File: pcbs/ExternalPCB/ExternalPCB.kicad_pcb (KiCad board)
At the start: 2 copper layers, 58.4 x 127 mm, 31 parts, among them J1 Bat +, J10 Conn_01x04_Pin, J11 Conn_01x04_Pin, J2 Bat -, J3 Conn_01x04_Pin, J4 Conn_01x05_Pin, J5 Conn_01x05_Pin, J6 Conn_01x03_Pin, J7 Conn_01x03_Pin, J8 Conn_01x04_Pin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

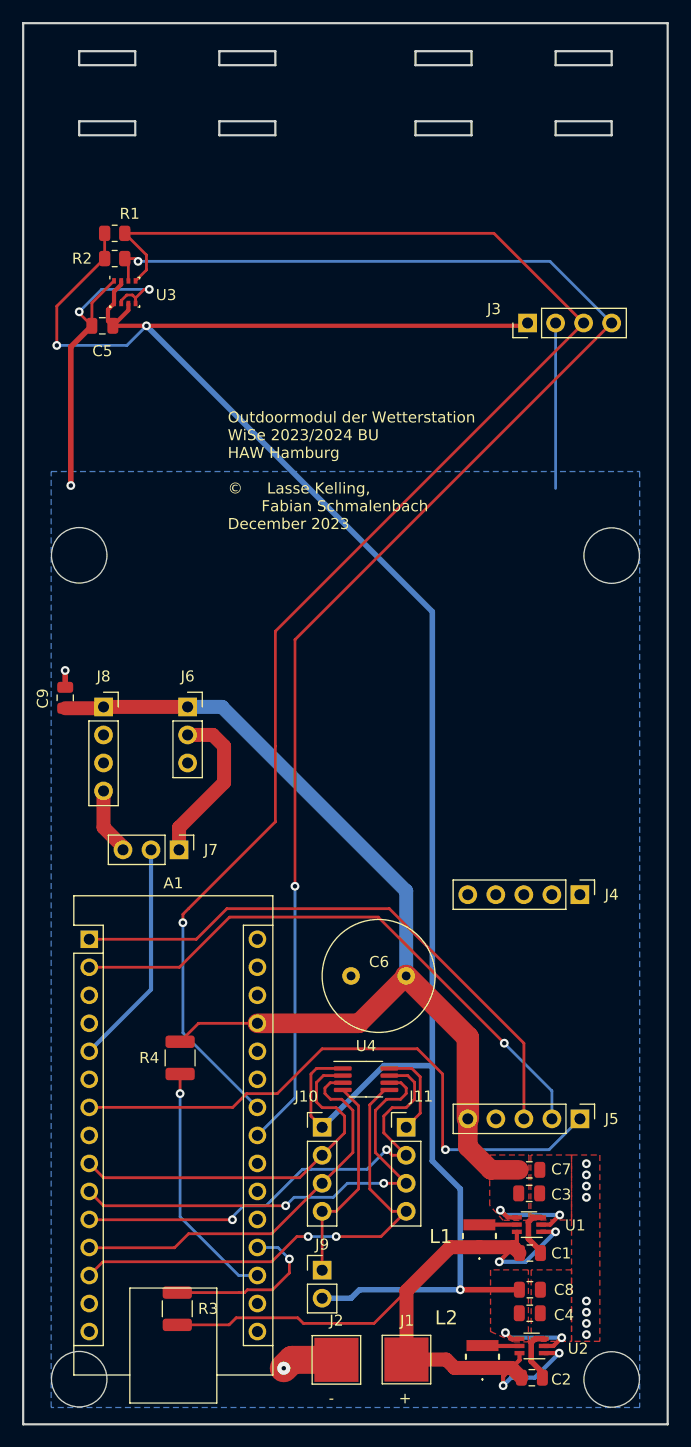
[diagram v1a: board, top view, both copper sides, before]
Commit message: JLCPCB hatte ein paar Teile nicht...
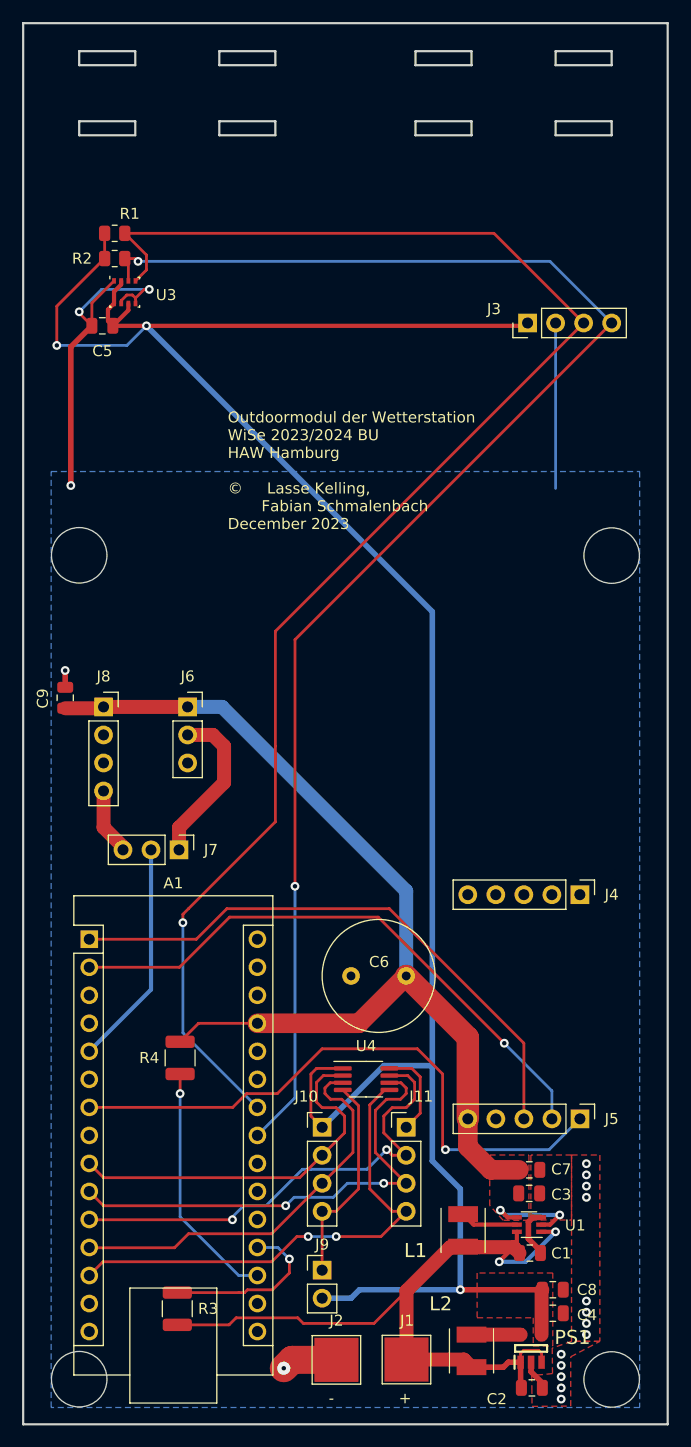
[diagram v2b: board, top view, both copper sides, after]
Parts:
- removed U2: TPS61221DCK, Package_TO_SOT_SMD:Texas_R-PDSO-G6
- added PS1: TPS61097A-33DBVR, TPS61097A:SOT95P280X145-5N, F.Cu at (91.5, 144.8)
- L1, L2: value EPL3015-472MLC -> LQH44PN4R7MJ0L; footprint EPL3015:EPL3015472MLC -> LQH44PN4R7MJ0L:LQH44PN100MJ0L
- moved C4 2.09 mm to (93.5, 141.6)
- moved C8 2.08 mm to (93.5, 139.4)
- moved L1 1.56 mm to (85.3, 134.1)
- moved L2 1.12 mm to (86.1, 145.0)
- moved C2 0.92 mm to (91.6, 148.3)
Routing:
- net +BATT: track 74.8 -> 69.3 mm, vias 4 -> 2
- net +3.3V: track 213.4 -> 210.8 mm, vias 5 -> 3
- net -BATT: track 72.3 -> 70.2 mm, vias 13 -> 18
- net Net-(U1-L): track 3.40 -> 5.26 mm
- net Net-(PS1-L): track 3.37 -> 4.45 mm
